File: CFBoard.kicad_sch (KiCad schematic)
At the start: 3 parts, among them U1 STM32 Blue Pill, U2 Wemos D1 Mini, U3 GY-6500

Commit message: feat: layout all the components
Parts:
- added C1: 220 uF 35V, Capacitor_THT:CP_Radial_D6.3mm_P2.50mm, symbol Device:C_Polarized
- added C2: 470uF 16V, Capacitor_THT:CP_Radial_D5.0mm_P2.50mm, symbol Device:C_Polarized
- added C3: 100uF 25V, Capacitor_THT:CP_Radial_D5.0mm_P2.50mm, symbol Device:C_Polarized
- added C4, C5: 104 Ceramic, Capacitor_THT:C_Disc_D3.0mm_W1.6mm_P2.50mm, symbol Device:C
- added CONN1: JST 6 Pin, Connector_JST:JST_XH_B6B-XH-A_1x06_P2.50mm_Vertical, symbol JST_6pin:JST_XH_6pin
- added D2: 3MM RED LED, LED_THT:LED_D3.0mm, symbol Device:LED
- added R1: 1KR, Resistor_THT:R_Axial_DIN0207_L6.3mm_D2.5mm_P10.16mm_Horizontal, symbol Device:R
- added R2, R3: 100R, Resistor_THT:R_Axial_DIN0207_L6.3mm_D2.5mm_P10.16mm_Horizontal, symbol Device:R
- added R4: 330R, Resistor_THT:R_Axial_DIN0207_L6.3mm_D2.5mm_P10.16mm_Horizontal, symbol Device:R
- added REG1: MP1584, MP1584:MP1584, symbol mp1584:MP1584
- added U4: BMP180_5pin, BMP180:BMP180_5Pin, symbol bmp180:BMP180_5pin
- U1: footprint STM32_Footprints:YAAJ_BluePill_1 -> STM32_Footprints:YAAJ_BluePill_2
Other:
- moved on the sheet: U1, U2, U3

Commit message: feat: pcb layout
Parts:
- added R5: 100R, R_Axial_DIN0207_L6.3mm_D2.5mm_P7.62mm_Horizontal, symbol Device:R
- R1, R2, R3: footprint Resistor_THT:R_Axial_DIN0207_L6.3mm_D2.5mm_P10.16mm_Horizontal -> R_Axial_DIN0207_L6.3mm_D2.5mm_P7.62mm_Horizontal
- R4: footprint Resistor_THT:R_Axial_DIN0207_L6.3mm_D2.5mm_P10.16mm_Horizontal -> Resistor_THT:R_Axial_DIN0207_L6.3mm_D2.5mm_P7.62mm_Horizontal
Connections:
- net at C3.1: now also C4.1, C5.1, U1.38 (3V3), U2.16 (3.3V), U3.1 (VIN), U4.1 (VIN)
- net at C3.2: now also C2.2, C4.2, C5.2, D2.2 (A), REG1.4 (VOUT-), U1.39 (GND), U2.2 (GND), U3.2 (GND), U4.2 (GND)
- net at R4.1: now also D2.1 (K)
- net at R4.2: now also U2.14 (D7)
- net at U3.3 (SCL): now also U1.16 (PB8), U4.3 (SCL)
- net at U3.4 (SDA): now also U1.17 (PB9), U3.8 (INT), U4.4 (SDA), R5.1
- net at U1.14 (PB6): now also R2.1
- net at U1.15 (PB7): now also R3.1
- net at U1.25 (PA0): now also CONN1.3 (Signal_1)
- net at U1.26 (PA1): now also CONN1.4 (Signal_2)
- net at U1.27 (PA2): now also CONN1.5 (Signal_3)
- net at U1.28 (PA3): now also CONN1.6 (Signal_4)
- net at U1.33 (PB0): now also R5.2
- net at U1.37 (RST): now also R1.2
- net at REG1.1 (VIN+): now also C1.1, CONN1.1 (VIN)
- net at REG1.2 (VIN-): now also C1.2, CONN1.2 (GND)
- net at REG1.3 (VOUT+): now also C2.1, U2.1 (5V)
- net at R3.2: now also U2.8 (Tx)
- net at U2.12 (D5): now also R1.1
- net at U2.7 (Rx): now also R2.2
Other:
- moved on the sheet: C1, C2, C3, C4, C5, CONN1, D2, R1, R2, R3, R4, REG1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

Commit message: feat: wrap up version 1
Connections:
- net at C3.1, C4.1, U1.38 (3V3)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: now also C5.2; no longer C5.1
- net at C2.2, C3.2, C4.2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: now also C5.1; no longer C5.2
- net at U1.17 (PB9), U3.4 (SDA), U4.4 (SDA): no longer R5.1, U3.8 (INT)
- new net: R5.1, U3.8 (INT)
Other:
- moved on the sheet: R5, U4

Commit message: chore: fix trace
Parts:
- added D1: 1N5819, Diode_THT:D_DO-41_SOD81_P7.62mm_Horizontal, symbol Device:D
- added SW1: Slide Switch, Button_Switch_THT:SW_Slide-03_Wuerth-WS-SLTV_10x2.5x6.4_P2.54mm, symbol Switch:SW_SPST
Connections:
- net at C4.1, C5.2, U1.38 (3V3)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: now also D1.2 (A); no longer C3.1, U2.16 (3.3V)
- net at C1.1, REG1.1 (VIN+): now also SW1.2 (B); no longer CONN1.1 (VIN)
- new net: CONN1.1 (VIN), SW1.1 (A)
- new net: C3.1, D1.1 (K), U2.16 (3.3V)
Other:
- moved on the sheet: R5

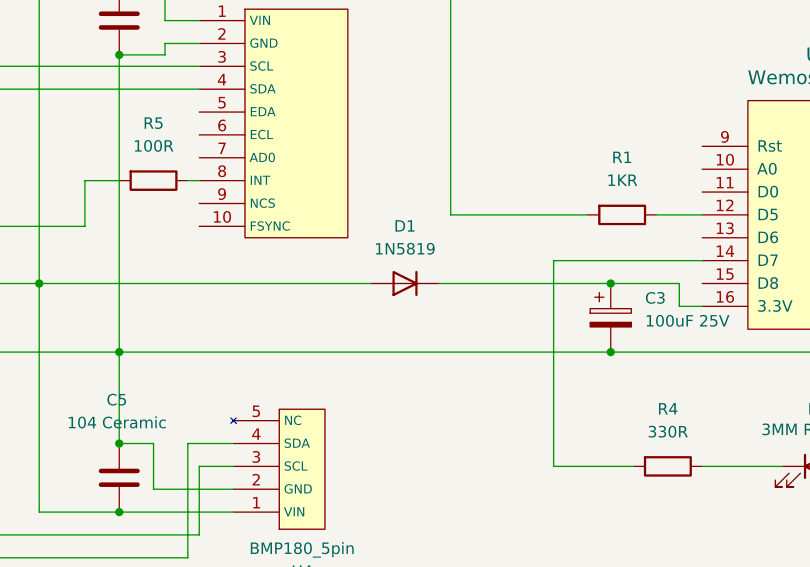
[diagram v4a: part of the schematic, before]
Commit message: feat: add silkscreen name and re-trace
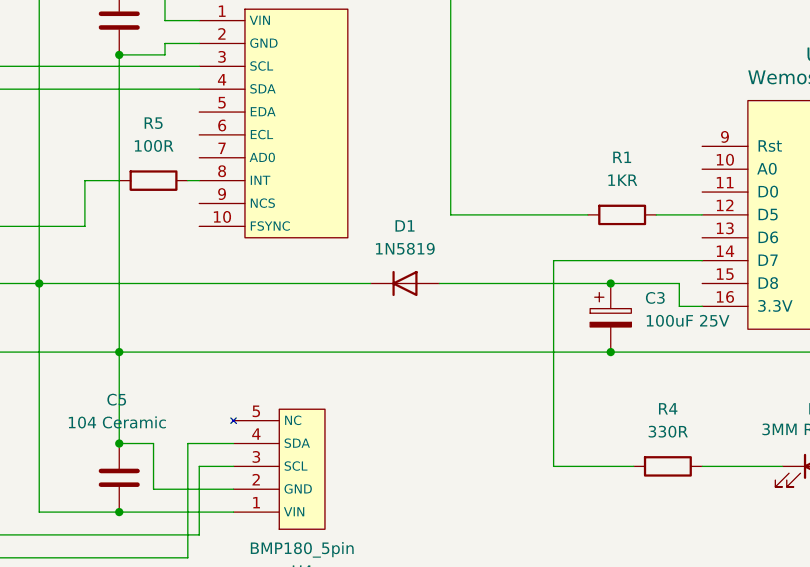
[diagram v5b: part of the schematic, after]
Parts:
- C4, C5: footprint Capacitor_THT:C_Disc_D3.0mm_W1.6mm_P2.50mm -> Capacitor_THT:C_Disc_D4.3mm_W1.9mm_P5.00mm
- CONN1: footprint Connector_JST:JST_XH_B6B-XH-A_1x06_P2.50mm_Vertical -> JST_XH_6Pin_Horizontal:JST_XH_6Pin_Horizontal
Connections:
- net at C3.1, U2.16 (3.3V): now also D1.2 (A); no longer D1.1 (K)
- net at C4.1, C5.2, U1.38 (3V3)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: now also D1.1 (K); no longer D1.2 (A)
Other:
- moved on the sheet: D1

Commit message: feat: generate gerbers
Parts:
- CONN1: footprint JST_XH_6Pin_Horizontal:JST_XH_6Pin_Horizontal -> Connector_JST:JST_XH_B6B-XH-A_1x06_P2.50mm_Vertical
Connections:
- net GNDPWR: now reaches C1.2, CONN1.2 (GND), REG1.2 (VIN-)
- no-connect marks 1 -> 42

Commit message: feat: update design
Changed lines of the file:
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@@
+	(wire
+		(pts
+			(xy 151.13 76.2) (xy 160.02 76.2)
+		)
+		(stroke
+			(width 0)
+			(type default)
+		)
+	)
 	(wire
 		(pts
@@
 	(wire
 		(pts
-			(xy 160.02 80.01) (xy 156.21 80.01)
-		)
-		(stroke
-			(width 0)
-			(type default)
-		)
-	)
-	(wire
-		(pts
 			(xy 142.24 134.62) (xy 151.13 134.62)
 		)
@@
 	(wire
 		(pts
-			(xy 156.21 76.2) (xy 151.13 76.2)
-		)
-		(stroke
-			(width 0)
-			(type default)
-		)
-	)
-	(wire
-		(pts
 			(xy 213.36 111.76) (xy 213.36 109.22)
 		)
@@
 	(wire
 		(pts
+			(xy 160.02 76.2) (xy 160.02 80.01)
+		)
+		(stroke
+			(width 0)
+			(type default)
+		)
+	)
+	(wire
+		(pts
 			(xy 133.35 85.09) (xy 133.35 137.16)
 		)
@@
 	(wire
 		(pts
+			(xy 142.24 76.2) (xy 151.13 76.2)
+		)
+		(stroke
+			(width 0)
+			(type default)
+		)
+	)
+	(wire
+		(pts
 			(xy 232.41 129.54) (xy 237.49 129.54)
 		)
@@
 	(wire
 		(pts
-			(xy 151.13 76.2) (xy 142.24 76.2)
-		)
-		(stroke
-			(width 0)
-			(type default)
-		)
-	)
-	(wire
-		(pts
 			(xy 118.11 40.64) (xy 114.3 40.64)
 		)
 		(stroke
-			(width 0)
-			(type default)
-		)
-	)
-	(wire
-		(pts
-			(xy 156.21 80.01) (xy 156.21 76.2)
-		)
-		(stroke

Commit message: feat: update jst connector footprint design
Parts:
- removed D1: 1N5819, Diode_THT:D_DO-41_SOD81_P7.62mm_Horizontal, symbol Device:D
- added D1: 1N5819, Diode_THT:D_DO-41_SOD81_P10.16mm_Horizontal, symbol Diode:1N5819
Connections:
- net at C3.1, U2.16 (3.3V): now also D1.2 (A)
- net at C4.1, C5.2, U1.38 (3V3)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: now also D1.1 (K)
